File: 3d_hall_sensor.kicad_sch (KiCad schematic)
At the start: 5 parts, among them U4 TMAG5173A2QDBVRQ1

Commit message: Edit symbol libraries for BOM
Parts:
- U4: MANUFACTURER Texas Instruments -> (none); MF Texas Instruments -> (none); MP TMAG5173A2QDBVRQ1 -> (none); Manufacturer (none) -> Texas Instruments; Part Number (none) -> TMAG5173A2QDBVRQ1
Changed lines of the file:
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@@
 			)
 		)
-		(property "MF" "Texas Instruments"
+		(property "Part Number" "TMAG5173A2QDBVRQ1"
 			(at 134.62 99.06 0)
 			(hide yes)
@@
 			)
 		)
-		(property "MP" "TMAG5173A2QDBVRQ1"
+		(property "Manufacturer" "Texas Instruments"
 			(at 134.62 99.06 0)
 			(hide yes)
-			(show_name no)
-			(do_not_autoplace no)
-			(effects
-				(font
-					(size 1.27 1.27)
-				)
-				(justify bottom)
-			)
-		)
-		(property "MANUFACTURER" "Texas Instruments"
-			(at 134.62 99.06 0)
-			(hide yes)

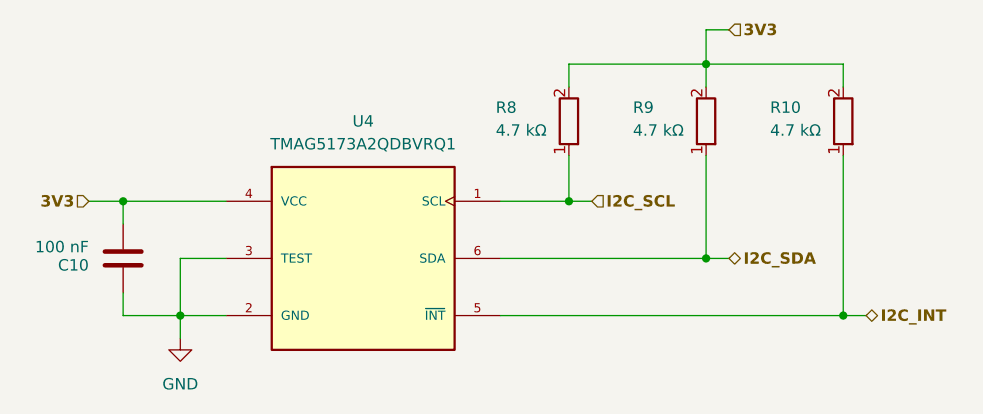
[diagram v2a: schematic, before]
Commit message: continued and finished conversion to ESP32-S3-WROOM module
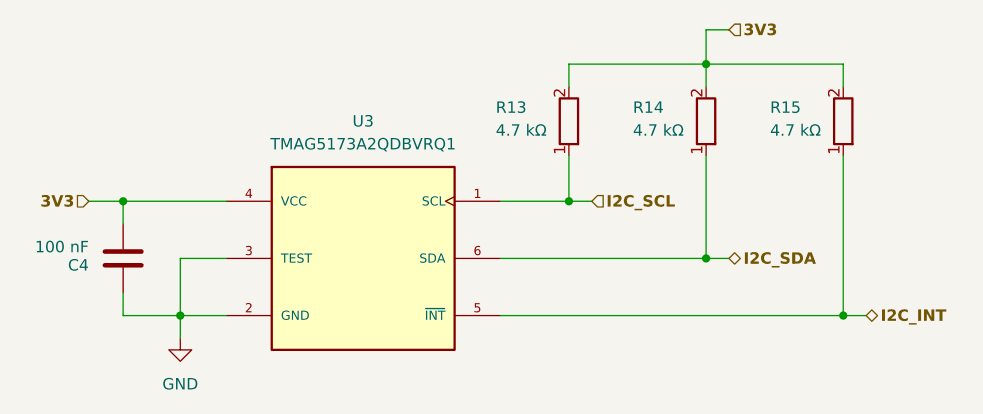
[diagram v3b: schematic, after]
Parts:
- renumbered C10 to C4, R8 to R13, R9 to R14, R10 to R15, U4 to U3
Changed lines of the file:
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@@
 		(dnp no)
 		(fields_autoplaced yes)
-		(property "Reference" "#PWR025"
+		(property "Reference" "#PWR024"
 			(at 114.3 114.3 0)
 			(hide yes)
@@
 			(project "Maglev"
 				(path "/cf460145-35f8-4019-907e-b966a2c32625/7adfdcc2-944c-4662-b790-50152b813ebf"
-					(reference "#PWR025")
+					(reference "#PWR024")
 					(unit 1)
 				)
@@
 		(dnp no)
 		(fields_autoplaced yes)
-		(property "Reference" "U4"
+		(property "Reference" "U3"
 			(at 134.62 83.82 0)
 			(show_name no)
@@
 			(project "Maglev"
 				(path "/cf460145-35f8-4019-907e-b966a2c32625/7adfdcc2-944c-4662-b790-50152b813ebf"
-					(reference "U4")
+					(reference "U3")
 					(unit 1)
 				)
@@
 		(in_pos_files yes)
 		(dnp no)
-		(property "Reference" "R9"
+		(property "Reference" "R14"
 			(at 164.592 82.296 90)
 			(show_name no)
@@
 			(project "Maglev"
 				(path "/cf460145-35f8-4019-907e-b966a2c32625/7adfdcc2-944c-4662-b790-50152b813ebf"
-					(reference "R9")
+					(reference "R14")
 					(unit 1)
 				)
@@
 		(in_pos_files yes)
 		(dnp no)
-		(property "Reference" "R10"
+		(property "Reference" "R15"
 			(at 179.832 82.296 90)
 			(show_name no)
@@
 			(project "Maglev"
 				(path "/cf460145-35f8-4019-907e-b966a2c32625/7adfdcc2-944c-4662-b790-50152b813ebf"
-					(reference "R10")
+					(reference "R15")
 					(unit 1)
 				)
@@
 		(in_pos_files yes)
 		(dnp no)
-		(property "Reference" "C10"
+		(property "Reference" "C4"
 			(at 104.14 99.8219 0)
 			(show_name no)
@@
 			(project "Maglev"
 				(path "/cf460145-35f8-4019-907e-b966a2c32625/7adfdcc2-944c-4662-b790-50152b813ebf"
-					(reference "C10")
+					(reference "C4")
 					(unit 1)
 				)
@@
 		(in_pos_files yes)
 		(dnp no)
-		(property "Reference" "R8"
+		(property "Reference" "R13"
 			(at 149.352 82.296 90)
 			(show_name no)
@@
 			(project "Maglev"
 				(path "/cf460145-35f8-4019-907e-b966a2c32625/7adfdcc2-944c-4662-b790-50152b813ebf"
-					(reference "R8")
+					(reference "R13")
 					(unit 1)
 				)
